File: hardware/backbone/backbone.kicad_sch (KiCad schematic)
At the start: 86 parts, among them J1 RESET, J10 CORE_A, J11 MOUNT, J13 FIELD_B, J14 FIELD_A, J15 UART PROG, J2 FROM_PREVIOUS, J4 FROM_PREVIOUS, J5 CONN_A, J6 BOOTLOADER, J7 CONN_B, J8 CORE_B, J9 TO NEXT, Q2 AO3401A, U11 470nH DCR=450m, U13 470nH DCR=450m, U15 ST25R100, U17 BLM18PG471SZ1D, U2 SN65HVD230DR, U4 AP2112K-3.3TRG1, U5 ESP32-C3-MINI-1-H4X, U8 G3VM-61VY3, U9 SN74AHCT1G14DCKR, X1 NX2016SA 27.12MHz

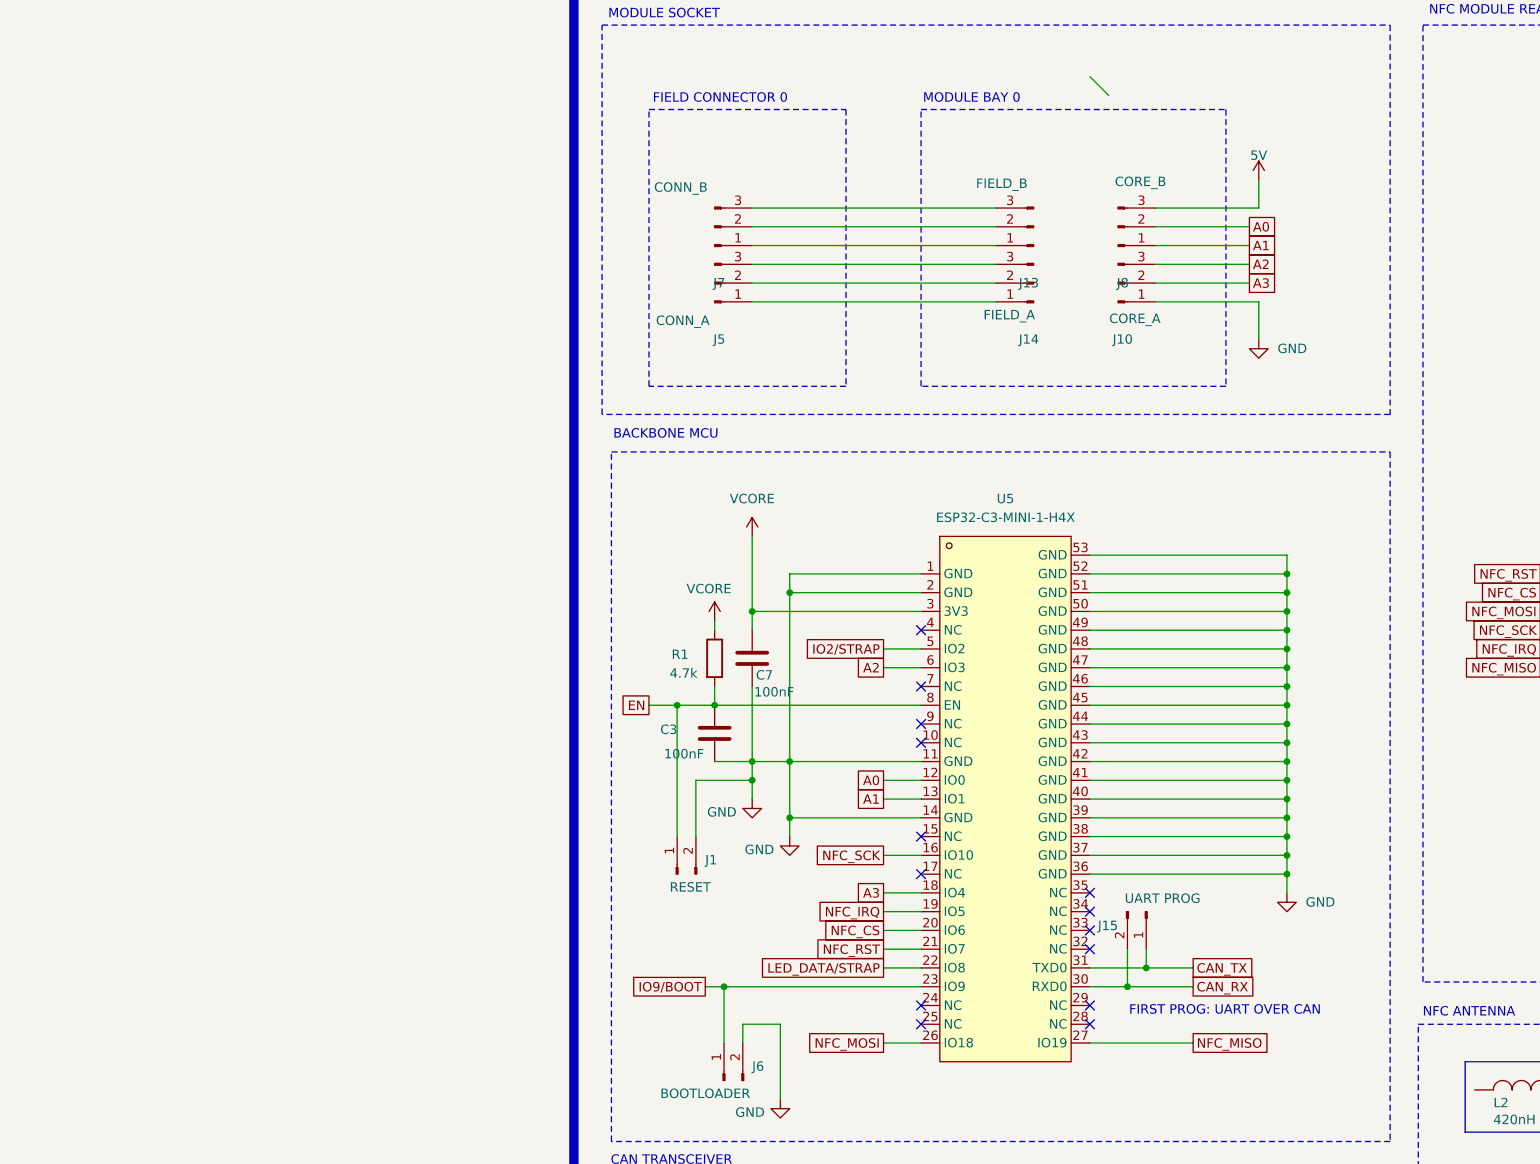
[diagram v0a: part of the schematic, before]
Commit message: fixed nfc via missing and some graphic changes to silkscreen for better readability
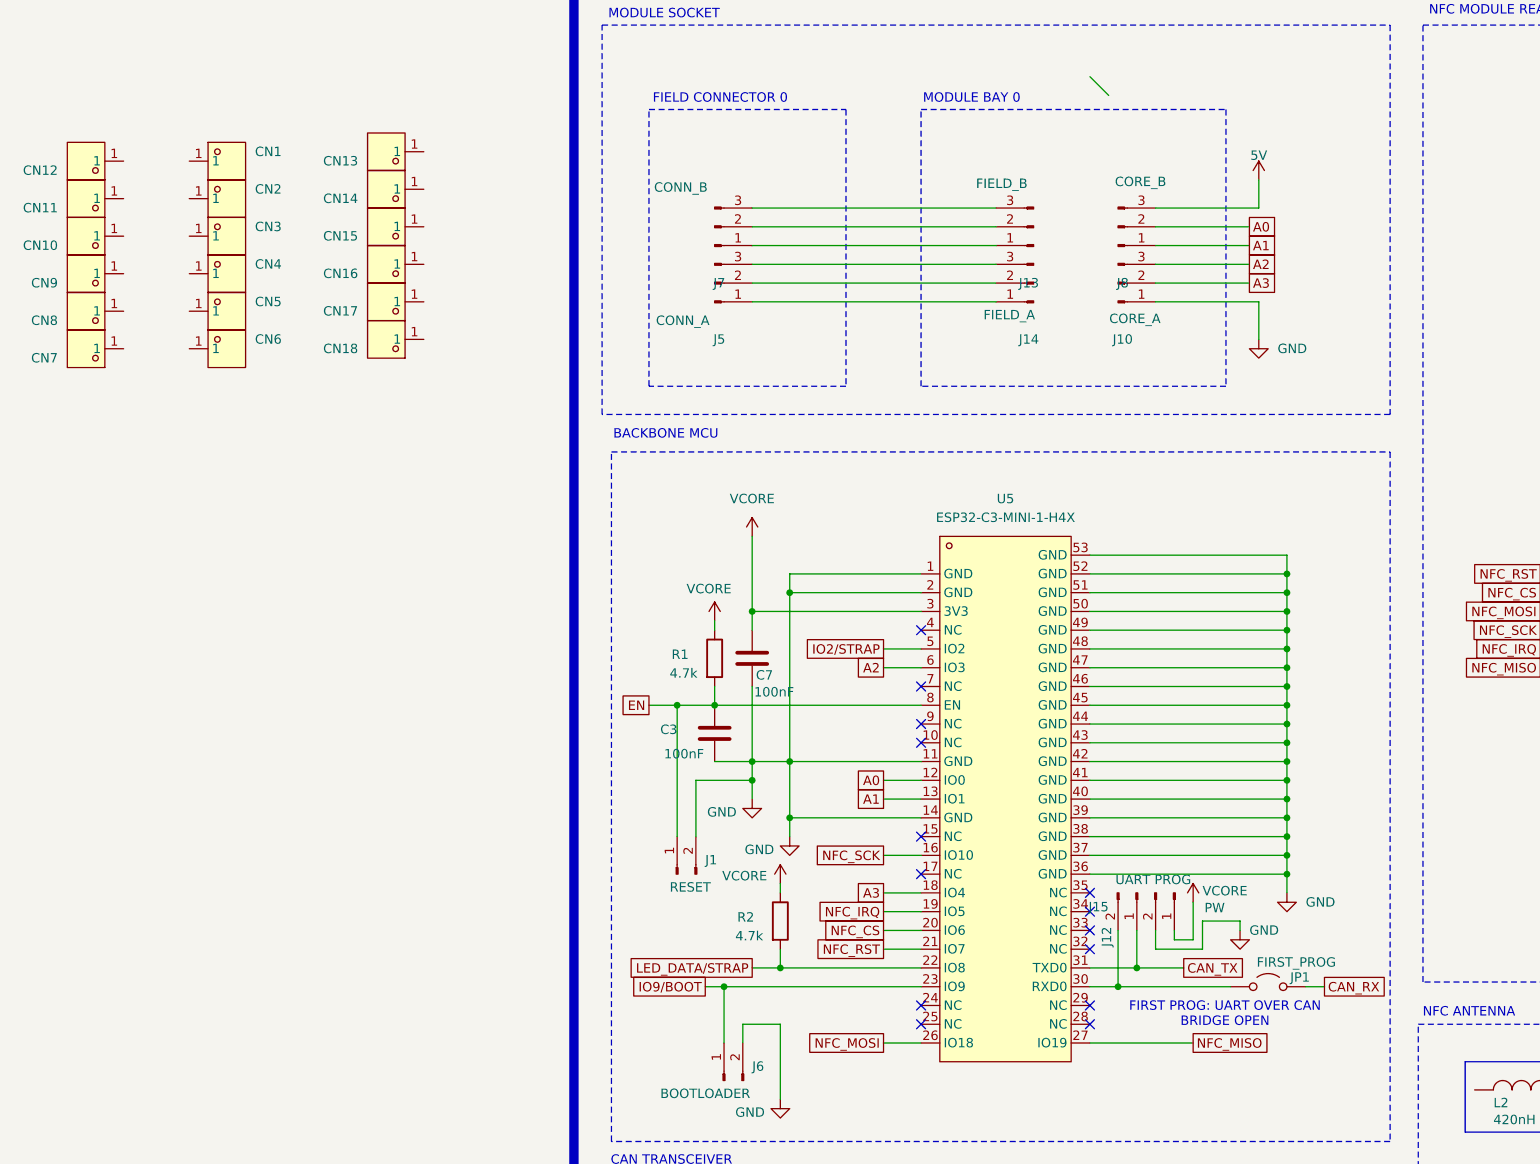
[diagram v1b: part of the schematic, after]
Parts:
- added CN1, CN10, CN11, CN12, CN13, CN14, CN15, CN16, CN17, CN18, CN2, CN3, CN4, CN5, CN6, CN7, CN8, CN9: BWCD-L6.5W2.0H2.0, SpaghettiLAB:SMD-1_BD2.0-H6.5, symbol SpaghettiLAB:BWCD-L6.5W2.0H2.0
- added J12: PW, Connector_PinHeader_2.54mm:PinHeader_1x02_P2.54mm_Vertical, symbol Connector:Conn_01x02_Pin
- added JP1: FIRST_PROG, Jumper:SolderJumper-2_P1.3mm_Open_RoundedPad1.0x1.5mm, symbol Jumper:Jumper_2_Open
- added R2: 4.7k, SpaghettiLAB2:R0603, symbol Device:R
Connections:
- net CAN_RX: now also JP1.2 (B); no longer J15.2 (Pin_2), U5.30 (RXD0)
- net GND: now also J12.2 (Pin_2)
- net LED_DATA/STRAP: now also R2.2
- net VCORE: now also J12.1 (Pin_1), R2.1
- new net: J15.2 (Pin_2), JP1.1 (A), U5.30 (RXD0)
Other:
- note added: "FIRST PROG: UART OVER CAN BRIDGE OPEN"
- note removed: "FIRST PROG: UART OVER CAN"
- moved on the sheet: J15

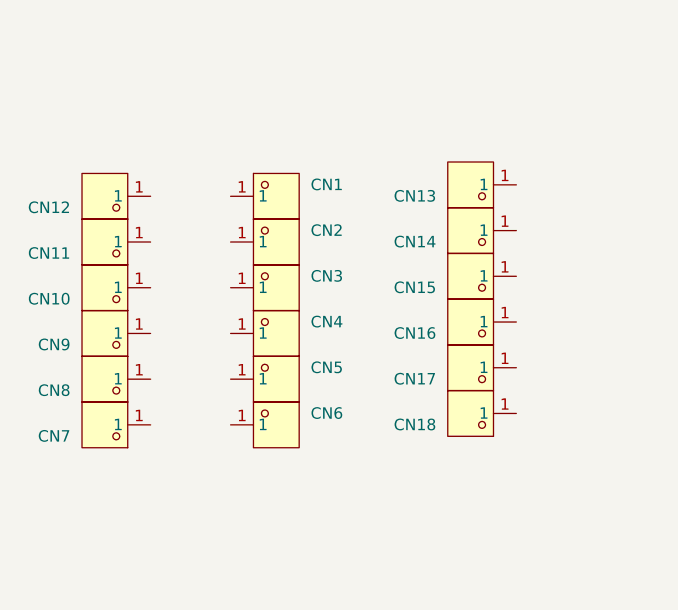
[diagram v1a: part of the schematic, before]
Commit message: fixed nfc via missing and some graphic changes to silkscreen for better readability
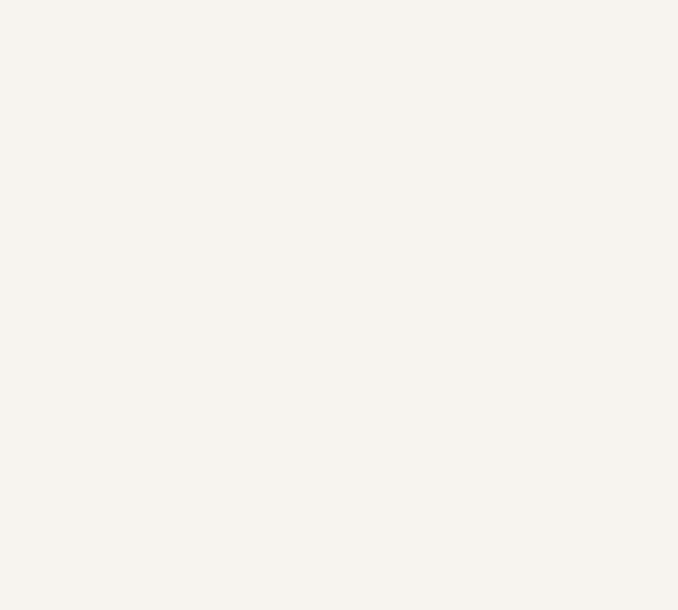
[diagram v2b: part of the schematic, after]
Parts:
- removed CN1, CN10, CN11, CN12, CN13, CN14, CN15, CN16, CN17, CN18, CN2, CN3, CN4, CN5, CN6, CN7, CN8, CN9: BWCD-L6.5W2.0H2.0, SpaghettiLAB:SMD-1_BD2.0-H6.5, symbol SpaghettiLAB:BWCD-L6.5W2.0H2.0

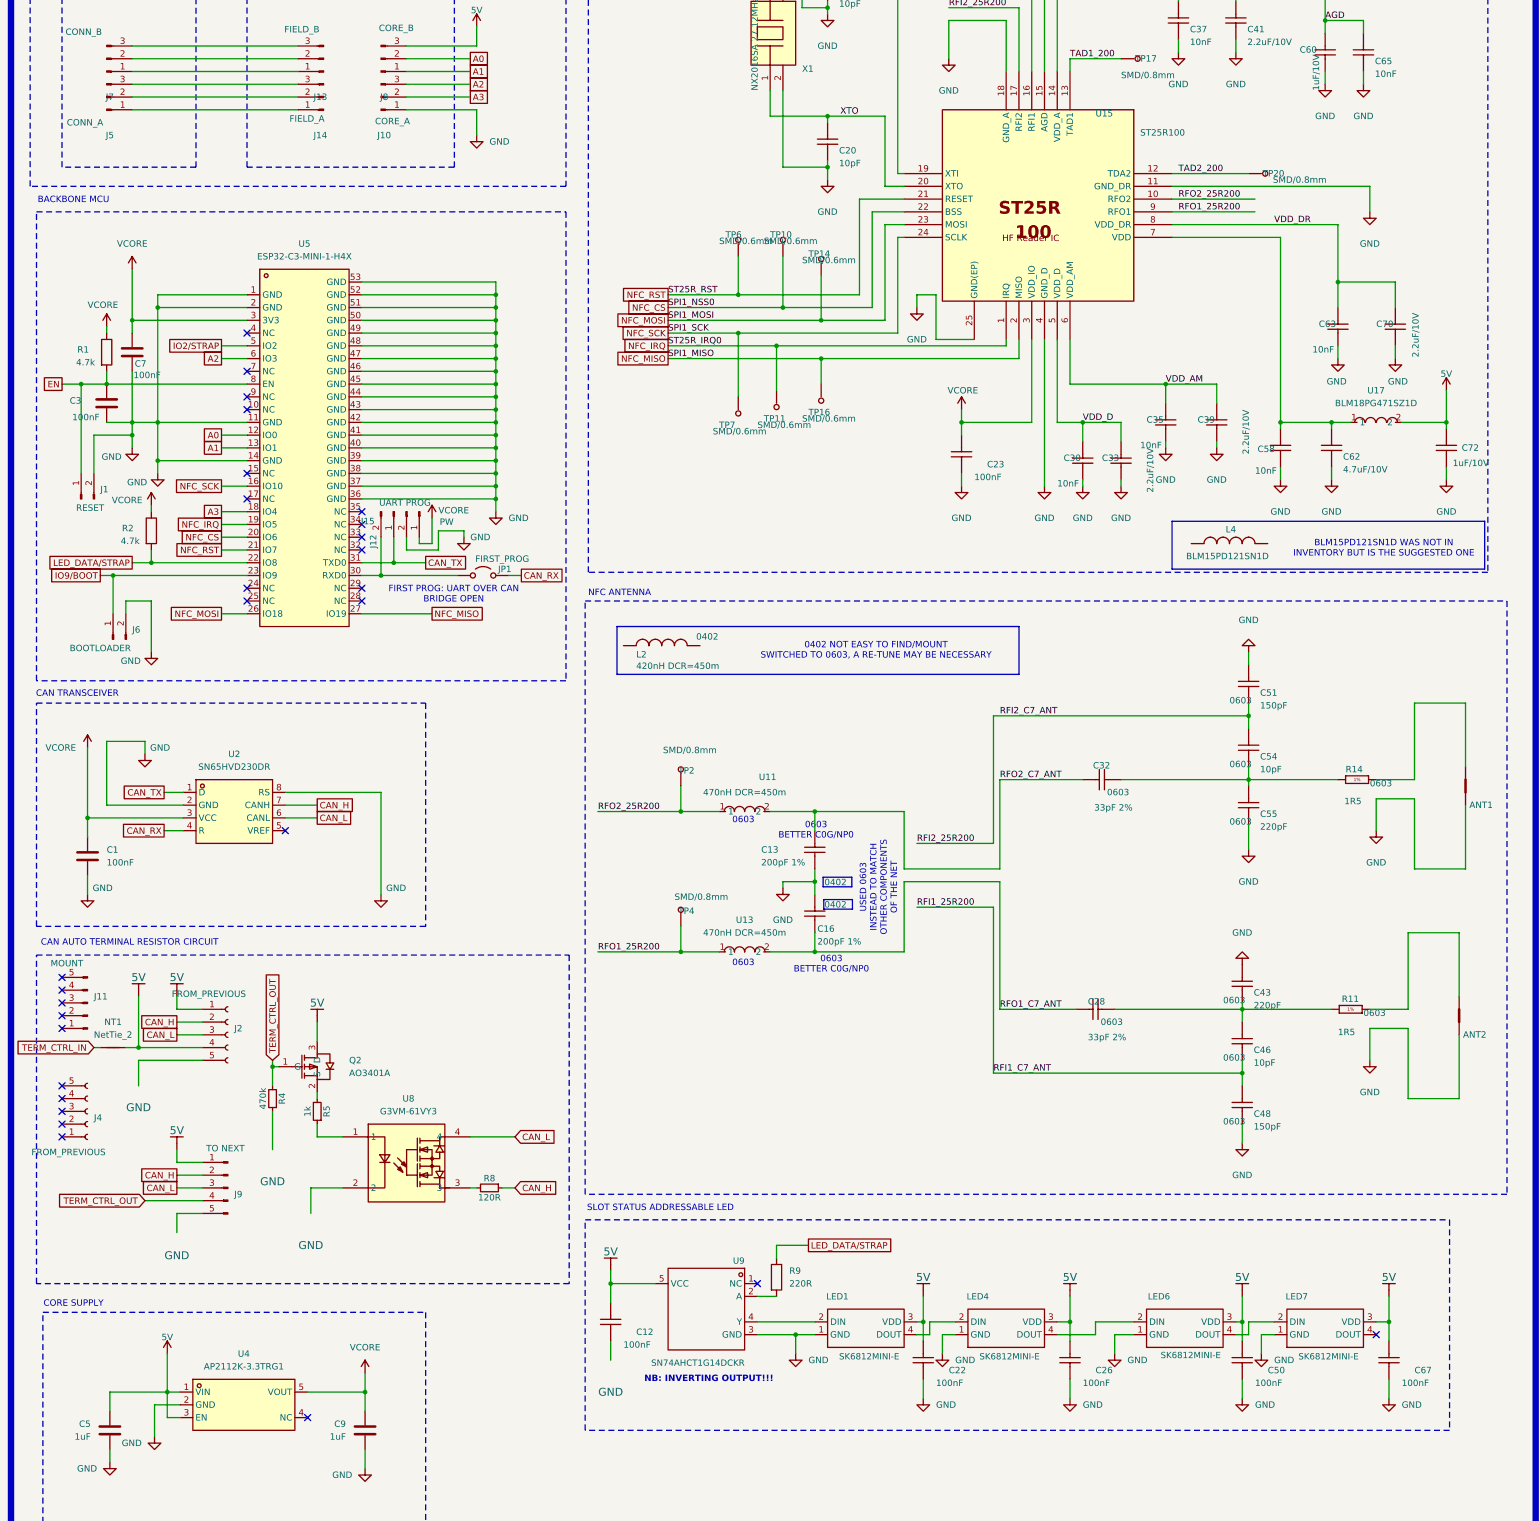
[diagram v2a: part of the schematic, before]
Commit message: Minor fix to utilities and hardware (backbone)
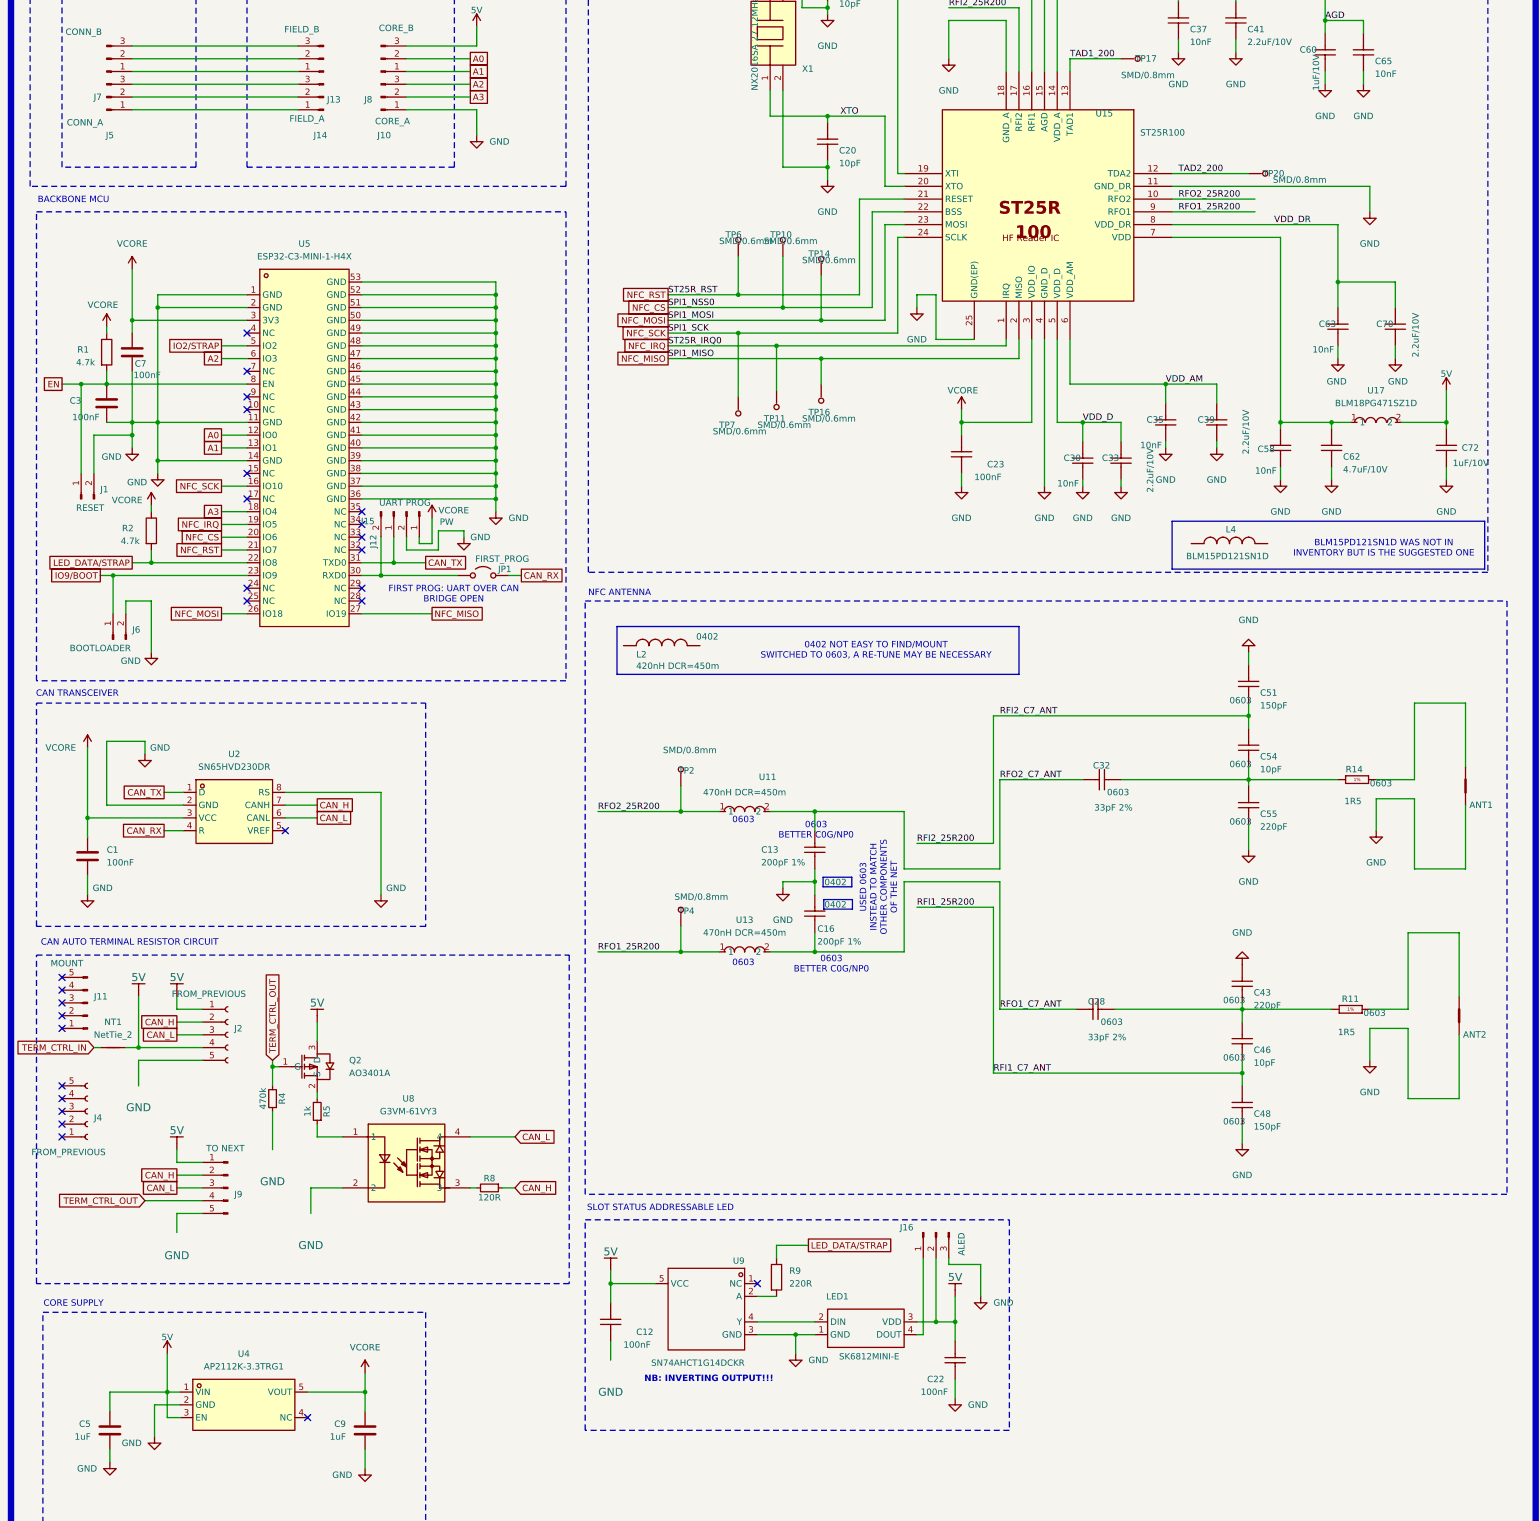
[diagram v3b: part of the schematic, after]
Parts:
- removed C26, C50, C67: 100nF, SpaghettiLAB2:C0603, symbol STMICRO:root_1_GRM033C71A104KE14D_STMICRO.SchLib
- removed LED4, LED6, LED7: SK6812MINI-E, SpaghettiLAB2:LED-SMD_4P-L3.2-W2.8-LS5.9_SK6812MINI-E, symbol USBC_PD_mo-easyedapro:SK6812MINI-E_C5149201
- added J16: ALED, Connector_PinSocket_2.54mm:PinSocket_1x03_P2.54mm_Vertical, symbol Connector:Conn_01x03_Pin
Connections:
- net 5V: now also J16.2 (Pin_2)
- net GND: now also J16.3 (Pin_3)
- net at LED1.4 (DOUT): now also J16.1 (Pin_1)
- no-connect marks 28 -> 27
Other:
- moved on the sheet: C22
